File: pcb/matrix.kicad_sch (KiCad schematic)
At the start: 0 parts

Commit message: kb matrix complete, stm32 wiring done
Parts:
- added D1, D10, D11, D12, D13, D14, D15, D16, D17, D18, D19, D2, D20, D21, D22, D23, D24, D25, D26, D27, D28, D29, D3, D30, D31, D32, D33, D34, D35, D36, D37, D38, D39, D4, D40, D41, D42, D43, D44, D45, D46, D47, D48, D49, D5, D50, D51, D52, D53, D54, D55, D56, D57, D58, D59, D6, D60, D61, D62, D63, D64, D65, D66, D67, D68, D69, D7, D70, D71, D72, D73, D74, D75, D76, D77, D78, D79, D8, D80, D81, D82, D83, D84, D85, D9: 1N4148W, Diode_SMD:D_SOD-123, symbol Diode:1N4148W
- added MX1, MX10, MX11, MX12, MX13, MX14, MX15, MX16, MX17, MX18, MX19, MX2, MX20, MX21, MX22, MX23, MX24, MX25, MX26, MX27, MX28, MX29, MX3, MX30, MX31, MX32, MX33, MX34, MX35, MX36, MX37, MX38, MX39, MX4, MX40, MX41, MX42, MX43, MX44, MX45, MX46, MX47, MX48, MX49, MX5, MX50, MX51, MX52, MX53, MX54, MX55, MX56, MX57, MX58, MX59, MX6, MX60, MX61, MX62, MX63, MX64, MX65, MX66, MX67, MX68, MX69, MX7, MX70, MX71, MX72, MX73, MX74, MX75, MX76, MX77, MX78, MX79, MX8, MX80, MX81, MX82, MX83, MX84, MX85, MX9: MX_SW_solder, PCM_marbastlib-mx:SW_MX_1u, symbol PCM_marbastlib-mx:MX_SW_solder
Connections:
- new net: D83.2 (A), MX83.2
- new net: D50.2 (A), MX50.2
- new net: D74.2 (A), MX74.2
- new net: D12.2 (A), MX12.2
- new net: D65.2 (A), MX65.2
- new net: D36.2 (A), MX36.2
- new net: D30.2 (A), MX30.2
- new net: D4.2 (A), MX4.2
- new net: D22.2 (A), MX22.2
- new net: D81.2 (A), MX81.2
- new net: D31.2 (A), MX31.2
- new net: D69.2 (A), MX69.2
- new net: D79.2 (A), MX79.2
- new net: D45.2 (A), MX45.2
- new net: D6.2 (A), MX6.2
- new net: D71.2 (A), MX71.2
- new net: D10.2 (A), MX10.2
- new net: D38.2 (A), MX38.2
- new net: D27.2 (A), MX27.2
- new net: D18.2 (A), MX18.2
- new net: D2.2 (A), MX2.2
- new net: D1.2 (A), MX1.2
- new net: D11.2 (A), MX11.2
- new net: D67.2 (A), MX67.2
- new net: D58.2 (A), MX58.2
- new net: D80.2 (A), MX80.2
- new net: D76.2 (A), MX76.2
- new net: D77.2 (A), MX77.2
- new net: D33.2 (A), MX33.2
- new net: D46.2 (A), MX46.2
- new net: D23.2 (A), MX23.2
- new net: D56.2 (A), MX56.2
- new net: D44.2 (A), MX44.2
- new net: D41.2 (A), MX41.2
- new net: D48.2 (A), MX48.2
- new net: D9.2 (A), MX9.2
- new net: D78.2 (A), MX78.2
- new net: D82.2 (A), MX82.2
- new net: D85.2 (A), MX85.2
- new net: D52.2 (A), MX52.2
- new net: D25.2 (A), MX25.2
- new net: D68.2 (A), MX68.2
- new net: D53.2 (A), MX53.2
- new net: D72.2 (A), MX72.2
- new net: D37.2 (A), MX37.2
- new net: D49.2 (A), MX49.2
- new net: D3.2 (A), MX3.2
- new net: D61.2 (A), MX61.2
- new net: D75.2 (A), MX75.2
- new net: D73.2 (A), MX73.2
- new net: D29.2 (A), MX29.2
- new net: D63.2 (A), MX63.2
- new net: D20.2 (A), MX20.2
- new net: D24.2 (A), MX24.2
- new net: D8.2 (A), MX8.2
- new net: D34.2 (A), MX34.2
- new net: D19.2 (A), MX19.2
- new net: D64.2 (A), MX64.2
- new net: D26.2 (A), MX26.2
- new net: D51.2 (A), MX51.2
- new net: D70.2 (A), MX70.2
- new net: D32.2 (A), MX32.2
- new net: D17.2 (A), MX17.2
- new net: D47.2 (A), MX47.2
- new net: D84.2 (A), MX84.2
- new net: D39.2 (A), MX39.2
- new net: D16.2 (A), MX16.2
- new net: D13.2 (A), MX13.2
- new net: D15.2 (A), MX15.2
- new net: D62.2 (A), MX62.2
- new net: D14.2 (A), MX14.2
- new net: D42.2 (A), MX42.2
- new net: D5.2 (A), MX5.2
- new net: D54.2 (A), MX54.2
- new net: D7.2 (A), MX7.2
- new net: D55.2 (A), MX55.2
- new net: D60.2 (A), MX60.2
- new net: D57.2 (A), MX57.2
- new net: D35.2 (A), MX35.2
- new net: D43.2 (A), MX43.2
- new net: D21.2 (A), MX21.2
- new net: D59.2 (A), MX59.2
- new net: D66.2 (A), MX66.2
- new net: D28.2 (A), MX28.2
- new net: D40.2 (A), MX40.2
- new net C1: MX1.1, MX17.1, MX34.1, MX48.1, MX61.1, MX74.1
- new net C10: MX26.1, MX43.1, MX57.1, MX70.1, MX9.1
- new net C11: MX10.1, MX27.1, MX44.1, MX58.1, MX71.1, MX80.1
- new net C12: MX11.1, MX28.1, MX45.1, MX59.1, MX72.1, MX81.1
- new net C13: MX12.1, MX29.1, MX46.1
- new net C14: MX13.1, MX30.1, MX47.1, MX60.1, MX82.1
- new net C15: MX14.1, MX31.1, MX83.1
- new net C16: MX15.1, MX32.1, MX73.1, MX84.1
- new net C17: MX16.1, MX33.1, MX85.1
- new net C2: MX18.1, MX2.1, MX35.1, MX49.1, MX62.1, MX75.1
- new net C3: MX19.1, MX3.1, MX36.1, MX50.1, MX63.1, MX76.1
- new net C4: MX20.1, MX37.1, MX4.1, MX51.1, MX64.1, MX77.1
- new net C5: MX21.1, MX38.1, MX5.1, MX52.1, MX65.1
- new net C6: MX22.1, MX39.1, MX53.1, MX66.1
- new net C7: MX23.1, MX40.1, MX54.1, MX6.1, MX67.1, MX78.1
- new net C8: MX24.1, MX41.1, MX55.1, MX68.1, MX7.1
- new net C9: MX25.1, MX42.1, MX56.1, MX69.1, MX79.1, MX8.1
- new net R1: D1.1 (K), D10.1 (K), D11.1 (K), D12.1 (K), D13.1 (K), D14.1 (K), D15.1 (K), D16.1 (K), D2.1 (K), D3.1 (K), D4.1 (K), D5.1 (K), D6.1 (K), D7.1 (K), D8.1 (K), D9.1 (K)
- new net R2: D17.1 (K), D18.1 (K), D19.1 (K), D20.1 (K), D21.1 (K), D22.1 (K), D23.1 (K), D24.1 (K), D25.1 (K), D26.1 (K), D27.1 (K), D28.1 (K), D29.1 (K), D30.1 (K), D31.1 (K), D32.1 (K), D33.1 (K)
- new net R3: D34.1 (K), D35.1 (K), D36.1 (K), D37.1 (K), D38.1 (K), D39.1 (K), D40.1 (K), D41.1 (K), D42.1 (K), D43.1 (K), D44.1 (K), D45.1 (K), D46.1 (K), D47.1 (K)
- new net R4: D48.1 (K), D49.1 (K), D50.1 (K), D51.1 (K), D52.1 (K), D53.1 (K), D54.1 (K), D55.1 (K), D56.1 (K), D57.1 (K), D58.1 (K), D59.1 (K), D60.1 (K)
- new net R5: D61.1 (K), D62.1 (K), D63.1 (K), D64.1 (K), D65.1 (K), D66.1 (K), D67.1 (K), D68.1 (K), D69.1 (K), D70.1 (K), D71.1 (K), D72.1 (K), D73.1 (K)
- new net R6: D74.1 (K), D75.1 (K), D76.1 (K), D77.1 (K), D78.1 (K), D79.1 (K), D80.1 (K), D81.1 (K), D82.1 (K), D83.1 (K), D84.1 (K), D85.1 (K)

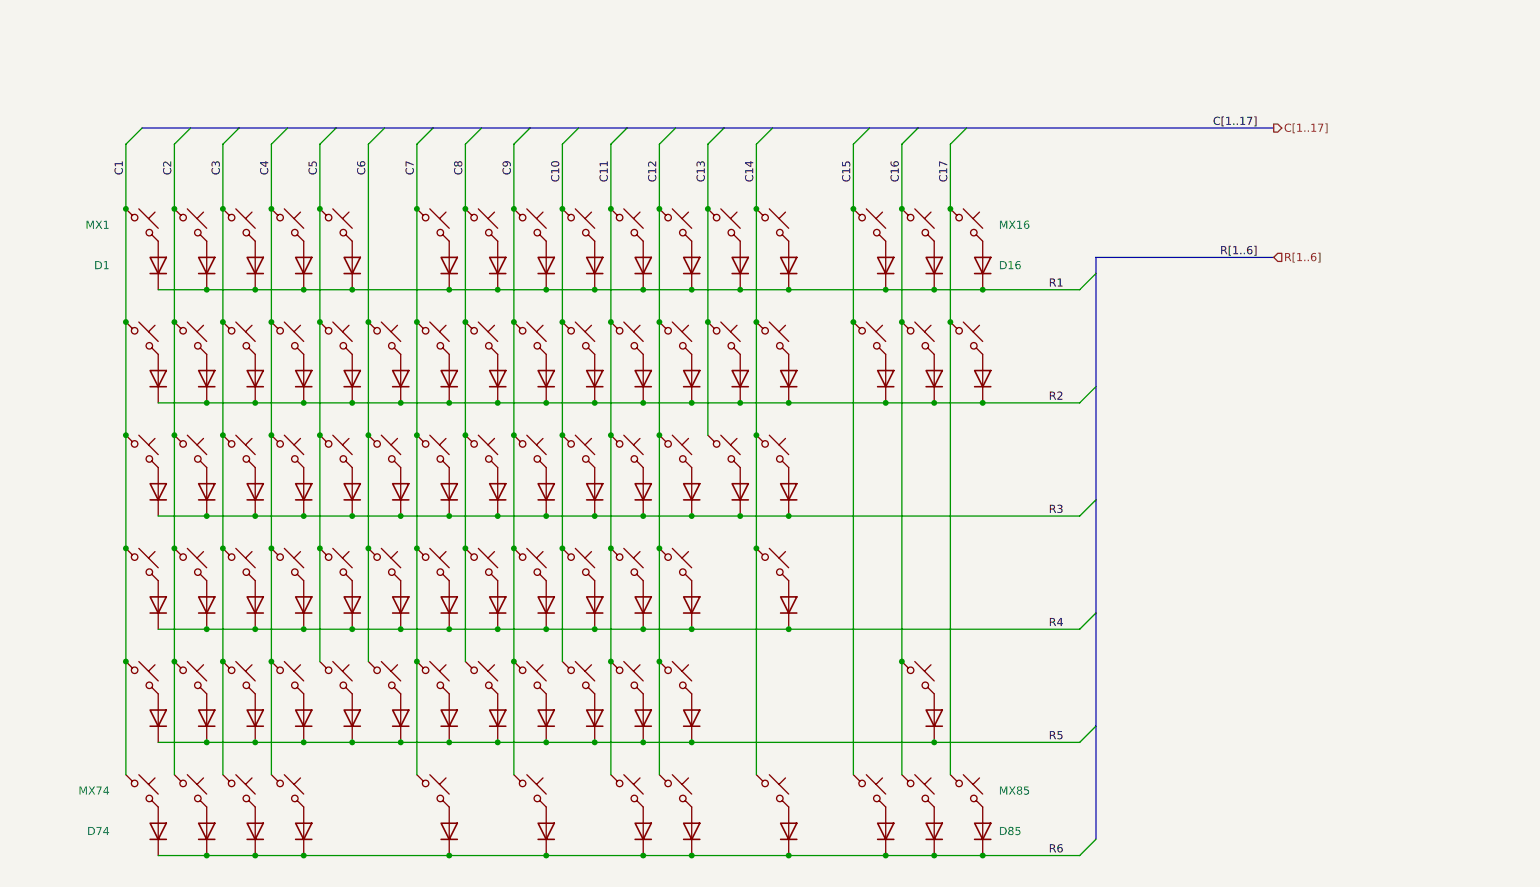
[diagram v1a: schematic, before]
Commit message: replaced usb c with molex for udb
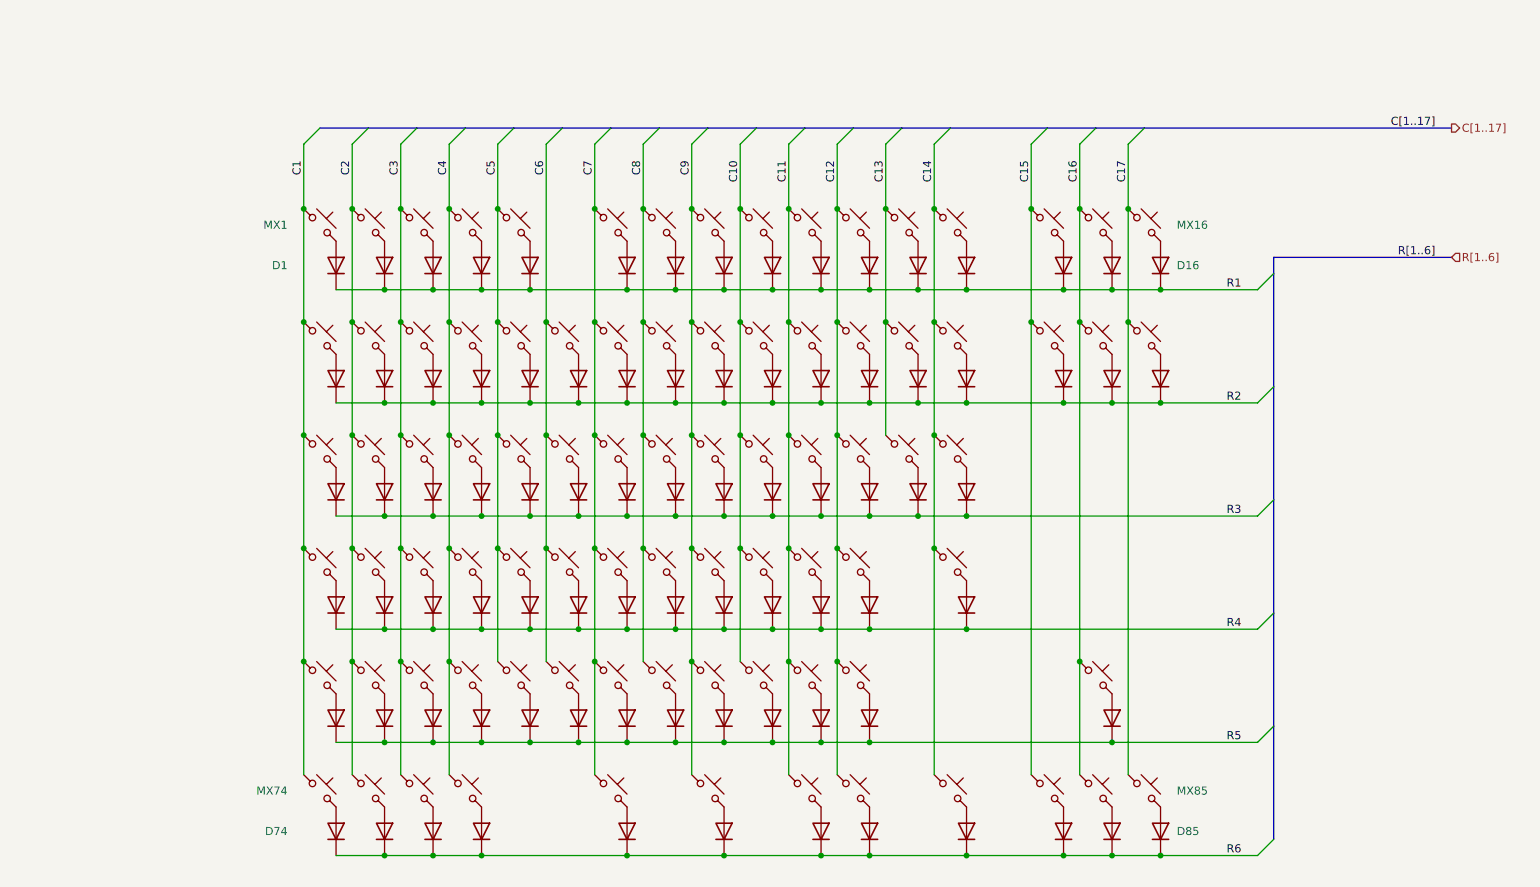
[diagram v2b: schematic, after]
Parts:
- D1, D10, D11, D12, D13, D14, D15, D16, D17, D18, D19, D2, D20, D21, D22, D23, D24, D25, D26, D27, D28, D29, D3, D30, D31, D32, D33, D34, D35, D36, D37, D38, D39, D4, D40, D41, D42, D43, D44, D45, D46, D47, D48, D49, D5, D50, D51, D52, D53, D54, D55, D56, D57, D58, D59, D6, D60, D61, D62, D63, D64, D65, D66, D67, D68, D69, D7, D70, D71, D72, D73, D74, D75, D76, D77, D78, D79, D8, D80, D81, D82, D83, D84, D85, D9: Manufacturer (none) -> Vishay General Semiconductor - Diodes Division; Manufacturer Product Number (none) -> 1N4148W-G3-08
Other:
- moved on the sheet: D1, D16, D74, D85, MX1, MX16, MX74, MX85

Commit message: reroute matrix
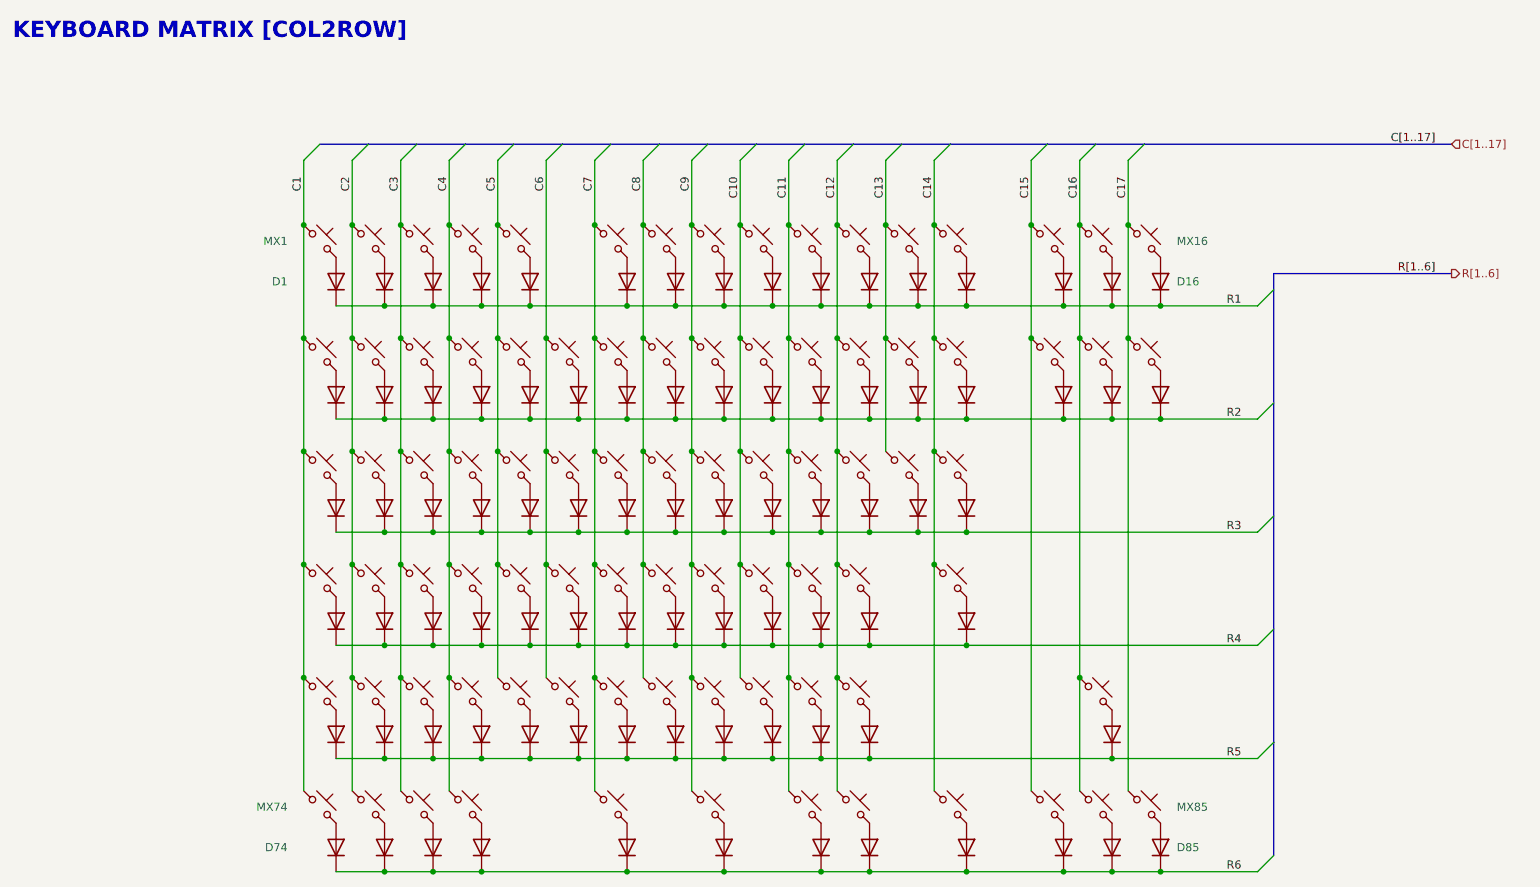
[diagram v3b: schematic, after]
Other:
- note added: "KEYBOARD MATRIX [COL2ROW]"
- company: (none) -> ASE, ASW, AMB
- title: (none) -> ALANA-KB PCB
- moved on the sheet: D1, D16, D74, D85, MX1, MX16, MX74, MX85
